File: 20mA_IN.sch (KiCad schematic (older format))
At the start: 10 parts, among them U2 LM324, U3 PC817, U4 PC817

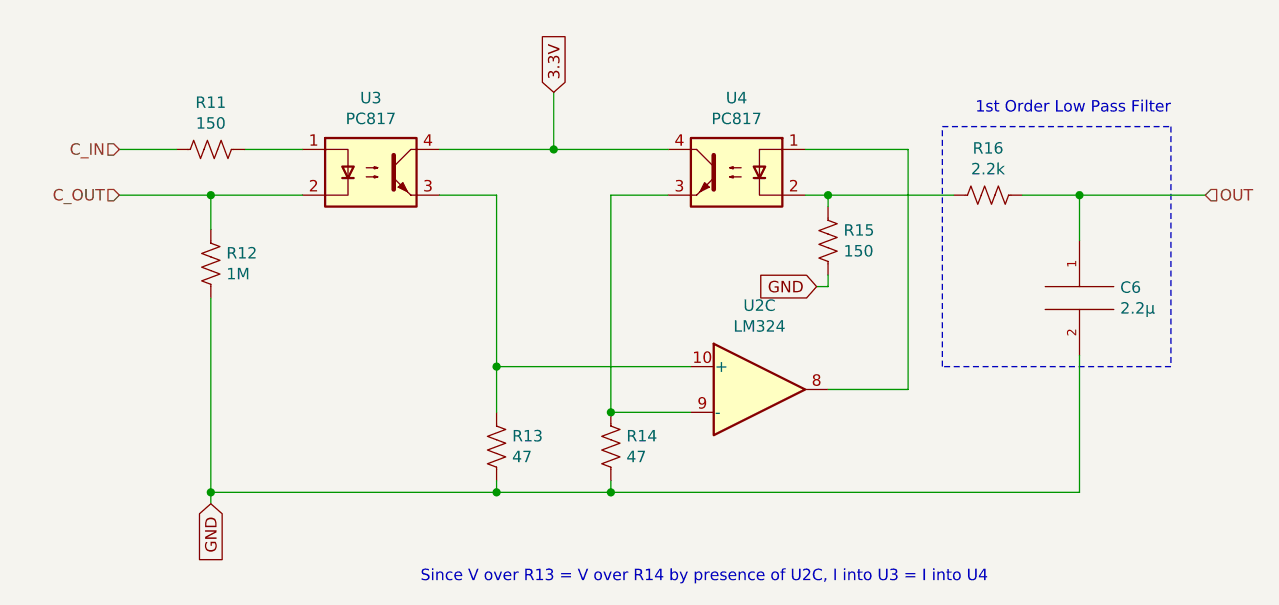
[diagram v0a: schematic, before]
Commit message: Finished 1st revision of 24V digital output circuit
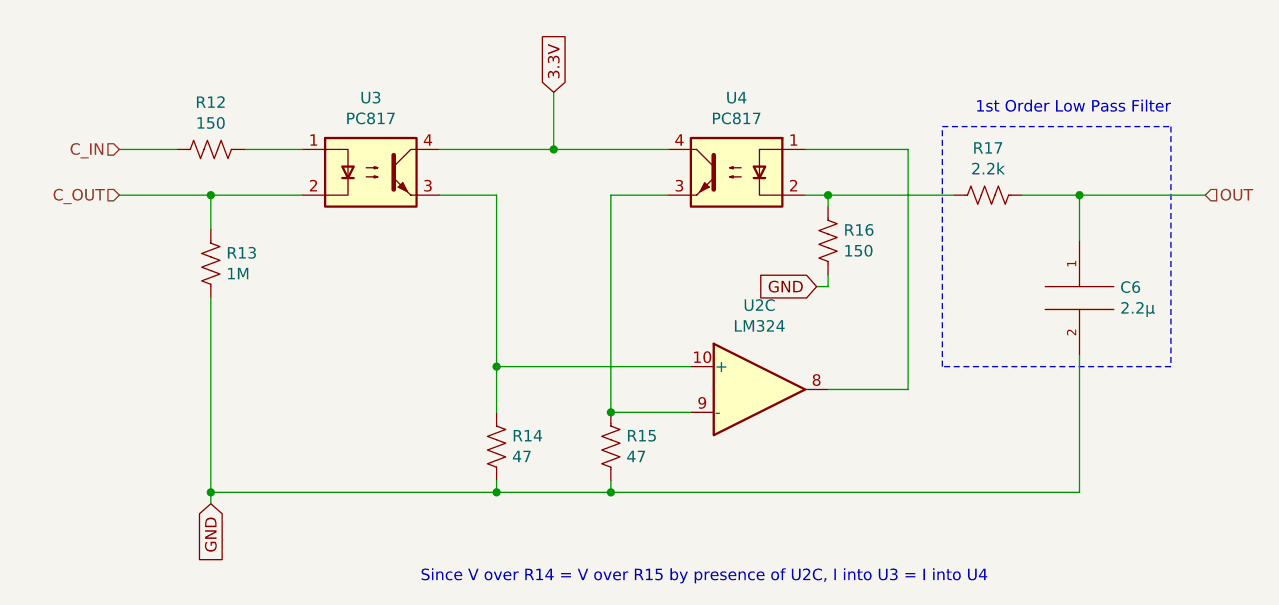
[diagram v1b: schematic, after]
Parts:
- renumbered R11 to R12, R12 to R13, R13 to R14, R14 to R15, R15 to R16, R16 to R17
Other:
- note added: "Since V over R14 = V over R15 by presence of U2C, I into U3 = I into U4"
- note removed: "Since V over R13 = V over R14 by presence of U2C, I into U3 = I into U4"
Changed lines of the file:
@@
 $EndDescr
 $Comp
-L Device:R_US R11
+L Device:R_US R12
 U 1 1 60AC4764
 P 4200 3350
-F 0 "R11" V 3995 3350 50  0000 C CNN
+F 0 "R12" V 3995 3350 50  0000 C CNN
 F 1 "150" V 4086 3350 50  0000 C CNN
 F 2 "Resistor_THT:R_Axial_DIN0207_L6.3mm_D2.5mm_P10.16mm_Horizontal" V 4240 3340 50  0001 C CNN
@@
 C_OUT
 $Comp
-L Device:R_US R12
+L Device:R_US R13
 U 1 1 60AC67AD
 P 4200 3850
-F 0 "R12" H 4132 3804 50  0000 R CNN
+F 0 "R13" H 4132 3804 50  0000 R CNN
 F 1 "1M" H 4132 3895 50  0000 R CNN
 F 2 "Resistor_THT:R_Axial_DIN0207_L6.3mm_D2.5mm_P10.16mm_Horizontal" V 4240 3840 50  0001 C CNN
@@
 $EndComp
 $Comp
-L Device:R_US R14
+L Device:R_US R15
 U 1 1 60ACED9B
 P 5950 4650
-F 0 "R14" H 5882 4604 50  0000 R CNN
+F 0 "R15" H 5882 4604 50  0000 R CNN
 F 1 "47" H 5882 4695 50  0000 R CNN
 F 2 "Resistor_THT:R_Axial_DIN0207_L6.3mm_D2.5mm_P10.16mm_Horizontal" V 5990 4640 50  0001 C CNN
@@
 $EndComp
 $Comp
-L Device:R_US R13
+L Device:R_US R14
 U 1 1 60ACF42F
 P 5450 4650
-F 0 "R13" H 5382 4604 50  0000 R CNN
+F 0 "R14" H 5382 4604 50  0000 R CNN
 F 1 "47" H 5382 4695 50  0000 R CNN
 F 2 "Resistor_THT:R_Axial_DIN0207_L6.3mm_D2.5mm_P10.16mm_Horizontal" V 5490 4640 50  0001 C CNN
@@
 Connection ~ 5950 4850
 $Comp
-L Device:R_US R15
+L Device:R_US R16
 U 1 1 60AD8205
 P 6900 3750
-F 0 "R15" H 6832 3704 50  0000 R CNN
+F 0 "R16" H 6832 3704 50  0000 R CNN
 F 1 "150" H 6832 3795 50  0000 R CNN
 F 2 "Resistor_THT:R_Axial_DIN0207_L6.3mm_D2.5mm_P10.16mm_Horizontal" V 6940 3740 50  0001 C CNN
@@
 $EndComp
 $Comp
-L Device:R_US R16
+L Device:R_US R17
 U 1 1 60ADC110
 P 7600 3550
-F 0 "R16" V 7395 3550 50  0000 C CNN
+F 0 "R17" V 7395 3550 50  0000 C CNN
 F 1 "2.2k" V 7486 3550 50  0000 C CNN
 F 2 "Resistor_THT:R_Axial_DIN0207_L6.3mm_D2.5mm_P10.16mm_Horizontal" V 7640 3540 50  0001 C CNN
@@
 Connection ~ 6900 3550
 Text Notes 7600 5250 2    50   ~ 0
-Since V over R13 = V over R14 by presence of U2C, I into U3 = I into U4
+Since V over R14 = V over R15 by presence of U2C, I into U3 = I into U4
 Wire Notes Line
 	7400 3250 8400 3250

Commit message: Cleanup and ERC compliance. Probably ready for Pcbnew after footprint association is done.
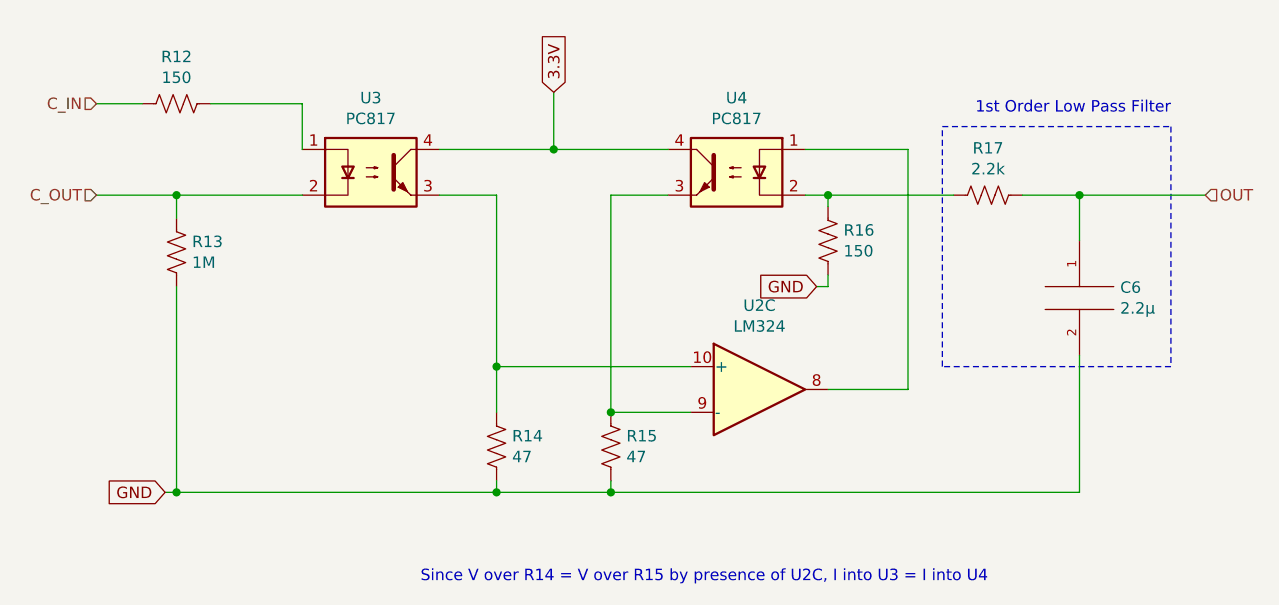
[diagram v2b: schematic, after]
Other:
- moved on the sheet: R12, R13
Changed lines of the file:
@@
 L Device:R_US R12
 U 1 1 60AC4764
-P 4200 3350
-F 0 "R12" V 3995 3350 50  0000 C CNN
-F 1 "150" V 4086 3350 50  0000 C CNN
-F 2 "Resistor_THT:R_Axial_DIN0207_L6.3mm_D2.5mm_P10.16mm_Horizontal" V 4240 3340 50  0001 C CNN
-F 3 "~" H 4200 3350 50  0001 C CNN
-	1    4200 3350
+P 4050 3150
+F 0 "R12" V 3845 3150 50  0000 C CNN
+F 1 "150" V 3936 3150 50  0000 C CNN
+F 2 "Resistor_THT:R_Axial_DIN0207_L6.3mm_D2.5mm_P10.16mm_Horizontal" V 4090 3140 50  0001 C CNN
+F 3 "~" H 4050 3150 50  0001 C CNN
+	1    4050 3150
 	0    1    1    0
 $EndComp
-Text HLabel 3800 3350 0    50   Input ~ 0
+Text HLabel 3700 3150 0    50   Input ~ 0
 C_IN
-Text HLabel 3800 3550 0    50   Input ~ 0
+Text HLabel 3700 3550 0    50   Input ~ 0
 C_OUT
 $Comp
 L Device:R_US R13
 U 1 1 60AC67AD
-P 4200 3850
-F 0 "R13" H 4132 3804 50  0000 R CNN
-F 1 "1M" H 4132 3895 50  0000 R CNN
-F 2 "Resistor_THT:R_Axial_DIN0207_L6.3mm_D2.5mm_P10.16mm_Horizontal" V 4240 3840 50  0001 C CNN
-F 3 "~" H 4200 3850 50  0001 C CNN
-	1    4200 3850
+P 4050 3800
+F 0 "R13" H 3982 3754 50  0000 R CNN
+F 1 "1M" H 3982 3845 50  0000 R CNN
+F 2 "Resistor_THT:R_Axial_DIN0207_L6.3mm_D2.5mm_P10.16mm_Horizontal" V 4090 3790 50  0001 C CNN
+F 3 "~" H 4050 3800 50  0001 C CNN
+	1    4050 3800
 	-1   0    0    1
 $EndComp
@@
 	1    0    0    -1
 $EndComp
-Wire Wire Line
-	3800 3350 4050 3350
-Wire Wire Line
-	4350 3350 4600 3350
-Wire Wire Line
-	4600 3550 4200 3550
-Wire Wire Line
-	4200 3550 4200 3700
-Connection ~ 4200 3550
-Wire Wire Line
-	4200 3550 3800 3550
-Text GLabel 4200 4900 3    50   Input ~ 0
+Text GLabel 4000 4850 0    50   Input ~ 0
 GND
 $Comp
@@
 Wire Wire Line
 	5450 4850 5450 4800
-Wire Wire Line
-	4200 4850 5450 4850
 Connection ~ 5450 4850
-Wire Wire Line
-	4200 4900 4200 4850
-Connection ~ 4200 4850
-Wire Wire Line
-	4200 4850 4200 4000
 Text GLabel 5700 3100 1    50   Input ~ 0
 3.3V
@@
 	1    0    0    -1
 $EndComp
+Wire Wire Line
+	4600 3150 4600 3350
+Wire Wire Line
+	3900 3150 3700 3150
+Wire Wire Line
+	3700 3550 4050 3550
+Wire Wire Line
+	4050 3550 4050 3650
+Connection ~ 4050 3550
+Wire Wire Line
+	4050 3950 4050 4850
+Wire Wire Line
+	4050 4850 5450 4850
+Wire Wire Line
+	4000 4850 4050 4850
+Connection ~ 4050 4850
+Wire Wire Line
+	4050 3550 4600 3550
+Wire Wire Line
+	4200 3150 4600 3150
 $EndSCHEMATC
